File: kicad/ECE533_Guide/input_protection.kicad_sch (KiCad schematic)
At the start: 29 parts, among them J1 DC+ 72V, J3 DC- return, Q1 IPT015N10N5, Q2 IPT015N10N5, U12 LM5069MM-2, U13 VOM1271T, U22 TLV3012

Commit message: Stage 2: BOM from schematic, LCSC numbers, fix duplicate C114 (refs #2)
- kicad/tools/make_bom.py builds bom/PCB_BOM.xlsx (+ CSV) from the netlist;
  previous report BOM kept as a sheet, Digi-Key PNs carried over
- 47 LCSC numbers verified on lcsc.com; two unconfirmed Murata MPNs replaced
- check_netlist.py now also checks for duplicate reference designators
- Yageo part-number codes fixed (13K, 0R jumper)

Co-Authored-By: Claude Opus 5.5 <noreply@anthropic.com>
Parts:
- C70, C71: LCSC (none) -> C5370002; MPN GRM21BR72A105KA01L -> CC0805KKX7R0BB105; Manufacturer Murata -> YAGEO
- C72: LCSC (none) -> C77052
- C73: LCSC (none) -> C77055
- R47: MPN RC0603FR-0713K0L -> RC0603FR-0713KL
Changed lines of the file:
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@@
 		(property "Datasheet" "" (at 111.76 87.63 0) (hide yes) (effects (font (size 1.27 1.27))))
 		(property "Description" "Unpolarized capacitor" (at 111.76 87.63 0) (hide yes) (effects (font (size 1.27 1.27))))
-		(property "MPN" "GRM21BR72A105KA01L" (at 111.76 87.63 0) (hide yes) (effects (font (size 1.27 1.27))))
-		(property "Manufacturer" "Murata" (at 111.76 87.63 0) (hide yes) (effects (font (size 1.27 1.27))))
+		(property "MPN" "CC0805KKX7R0BB105" (at 111.76 87.63 0) (hide yes) (effects (font (size 1.27 1.27))))
+		(property "Manufacturer" "YAGEO" (at 111.76 87.63 0) (hide yes) (effects (font (size 1.27 1.27))))
+		(property "LCSC" "C5370002" (at 111.76 87.63 0) (hide yes) (effects (font (size 1.27 1.27))))
 		(pin "1")
 		(pin "2")
@@
 		(property "Datasheet" "" (at 127 105.41 0) (hide yes) (effects (font (size 1.27 1.27))))
 		(property "Description" "Unpolarized capacitor" (at 127 105.41 0) (hide yes) (effects (font (size 1.27 1.27))))
-		(property "MPN" "GRM21BR72A105KA01L" (at 127 105.41 0) (hide yes) (effects (font (size 1.27 1.27))))
-		(property "Manufacturer" "Murata" (at 127 105.41 0) (hide yes) (effects (font (size 1.27 1.27))))
+		(property "MPN" "CC0805KKX7R0BB105" (at 127 105.41 0) (hide yes) (effects (font (size 1.27 1.27))))
+		(property "Manufacturer" "YAGEO" (at 127 105.41 0) (hide yes) (effects (font (size 1.27 1.27))))
+		(property "LCSC" "C5370002" (at 127 105.41 0) (hide yes) (effects (font (size 1.27 1.27))))
 		(pin "1")
 		(pin "2")
@@
 		(property "MPN" "GRM188R71E474KA12D" (at 198.12 140.97 0) (hide yes) (effects (font (size 1.27 1.27))))
 		(property "Manufacturer" "Murata" (at 198.12 140.97 0) (hide yes) (effects (font (size 1.27 1.27))))
+		(property "LCSC" "C77052" (at 198.12 140.97 0) (hide yes) (effects (font (size 1.27 1.27))))
 		(pin "1")
 		(pin "2")
@@
 		(property "Datasheet" "" (at 208.28 140.97 0) (hide yes) (effects (font (size 1.27 1.27))))
 		(property "Description" "Resistor" (at 208.28 140.97 0) (hide yes) (effects (font (size 1.27 1.27))))
-		(property "MPN" "RC0603FR-0713K0L" (at 208.28 140.97 0) (hide yes) (effects (font (size 1.27 1.27))))
+		(property "MPN" "RC0603FR-0713KL" (at 208.28 140.97 0) (hide yes) (effects (font (size 1.27 1.27))))
 		(property "Manufacturer" "YAGEO" (at 208.28 140.97 0) (hide yes) (effects (font (size 1.27 1.27))))
 		(pin "1")
@@
 		(property "MPN" "GRM188R71H104KA93D" (at 340.36 54.61 0) (hide yes) (effects (font (size 1.27 1.27))))
 		(property "Manufacturer" "Murata" (at 340.36 54.61 0) (hide yes) (effects (font (size 1.27 1.27))))
-		(pin "1")
-		(pin "2")
+		(property "LCSC" "C77055" (at 340.36 54.61 0) (hide yes) (effects (font (size 1.27 1.27))))
+		(pin "1")
+		(pin "2")

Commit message: Stage 3: footprints from datasheets and vendor libraries, 3D-checked (refs #3)
- ECE533_Mods.pretty (drawn from manufacturer datasheets):
  EPC2304 (EPC copper, solder-mask-defined land pattern and stencil),
  TDK ERUC23 (TDK recommended layout), R_2512_Kelvin (Bourns CSS2H-2512
  pads with net-tie sense strips), Littelfuse 456 fuse (+ placeholder STEP)
- ECE533_Vendor library (git-ignored): Wurth REDCUBE 74650194R and the
  SamacSys NME1S0505SC footprint; vendor STEP models referenced from
  kicad/lib/vendor, alignment verified by rendering
- gen_footprints.py regenerates both libraries; check_footprints.py checks
  symbol pins against footprint pads
- Fix D15/D16 BAT54W footprint: SOT-323, not SOD-323 (pin 3 had no pad)
- ERC: 0 violations locally (footprint links now resolve)

Co-Authored-By: Claude Opus 5.5 <noreply@anthropic.com>
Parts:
- J1, J3: footprint ECE533_Mods:Wurth_REDCUBE_74650194 -> ECE533_Vendor:Wurth_REDCUBE_74650194
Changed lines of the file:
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@@
 		(property "Reference" "J1" (at 17.78 80.01 0) (effects (font (size 1.27 1.27)) (justify left)))
 		(property "Value" "DC+ 72V" (at 17.78 82.55 0) (effects (font (size 1.27 1.27)) (justify left)))
-		(property "Footprint" "ECE533_Mods:Wurth_REDCUBE_74650194" (at 35.56 81.28 0) (hide yes) (effects (font (size 1.27 1.27))))
+		(property "Footprint" "ECE533_Vendor:Wurth_REDCUBE_74650194" (at 35.56 81.28 0) (hide yes) (effects (font (size 1.27 1.27))))
 		(property "Datasheet" "" (at 35.56 81.28 0) (hide yes) (effects (font (size 1.27 1.27))))
 		(property "Description" "Generic connector, single row, 01x01, script generated (kicad-library-utils/schlib/autogen/connector/)" (at 35.56 81.28 0) (hide yes) (effects (font (size 1.27 1.27))))
@@
 		(property "Reference" "J3" (at 17.78 110.49 0) (effects (font (size 1.27 1.27)) (justify left)))
 		(property "Value" "DC- return" (at 17.78 113.03 0) (effects (font (size 1.27 1.27)) (justify left)))
-		(property "Footprint" "ECE533_Mods:Wurth_REDCUBE_74650194" (at 35.56 111.76 0) (hide yes) (effects (font (size 1.27 1.27))))
+		(property "Footprint" "ECE533_Vendor:Wurth_REDCUBE_74650194" (at 35.56 111.76 0) (hide yes) (effects (font (size 1.27 1.27))))
 		(property "Datasheet" "" (at 35.56 111.76 0) (hide yes) (effects (font (size 1.27 1.27))))
 		(property "Description" "Generic connector, single row, 01x01, script generated (kicad-library-utils/schlib/autogen/connector/)" (at 35.56 111.76 0) (hide yes) (effects (font (size 1.27 1.27))))

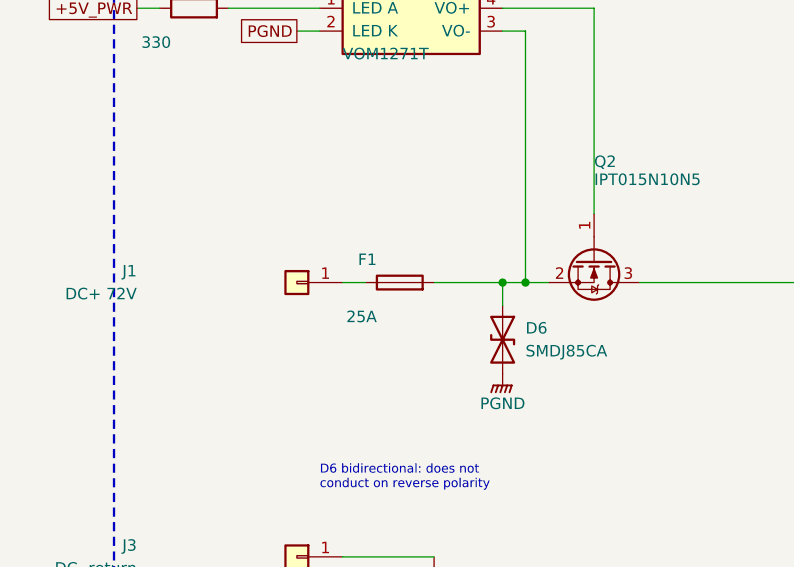
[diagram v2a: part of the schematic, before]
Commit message: Stage 3: input fuse F1 becomes a not-fitted option, R96 link (refs #3)
0456025.ER is rated 72 VDC, below the 79.2 V maximum input, and no
>=25 A SMD fuse rated >=100 VDC was found. Per review decision the
LM5069 circuit breaker is the eFuse; F1 keeps its NANO2 456 footprint
(DNP) and R96 (Bourns CSS2H-2512C-000, <0.1 mOhm, 100 A) links it.
Adds the R_2512_CSS2H footprint; BOM regenerated.

Co-Authored-By: Claude Opus 5.5 <noreply@anthropic.com>
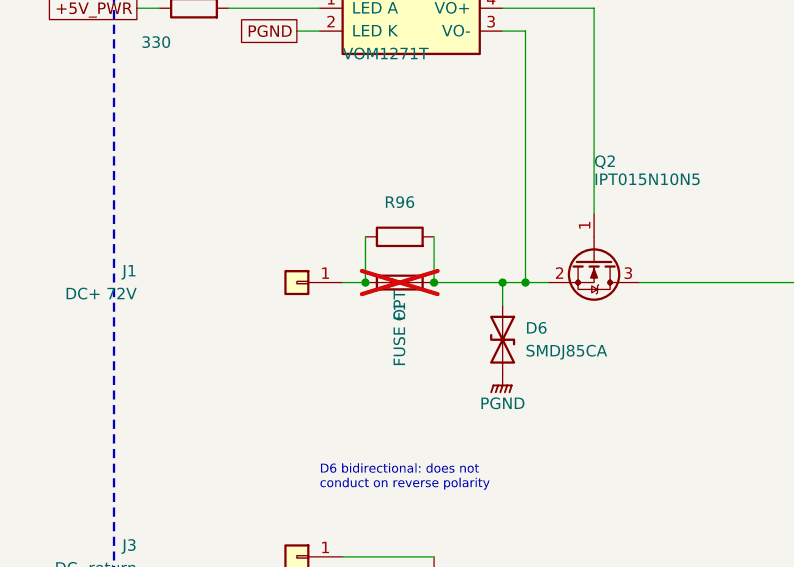
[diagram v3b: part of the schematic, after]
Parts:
- added R96: 0R 100A, ECE533_Mods:R_2512_CSS2H, symbol Device:R
- F1: value 25A -> FUSE OPT; LCSC C315877 -> (none); MPN 0456025.ER -> not fitted; Manufacturer Littelfuse -> (none); now not fitted
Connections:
- net at F1.1, J1.1 (Pin_1): now also R96.1
- net at D6.1 (A1), F1.2, Q2.2 (S)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: now also R96.2
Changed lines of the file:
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@@
 	)
 	(text "INPUT PROTECTION (HV domain):  J1 -> F1 -> D6 -> Q2 (reverse) -> RS1 -> Q1 (hot-swap) -> VBUS" (exclude_from_sim no) (at 20.32 20.32 0) (effects (font (size 1.778 1.778) (bold yes)) (justify left top)))
+	(wire (pts (xy 43.18 81.28) (xy 43.18 76.2)) (stroke (width 0) (type default)))
+	(junction (at 43.18 81.28) (diameter 0) (color 0 0 0 0))
+	(wire (pts (xy 50.8 81.28) (xy 50.8 76.2)) (stroke (width 0) (type default)))
+	(junction (at 50.8 81.28) (diameter 0) (color 0 0 0 0))
 	(wire (pts (xy 40.64 111.76) (xy 50.8 111.76)) (stroke (width 0) (type default)))
 	(wire (pts (xy 40.64 81.28) (xy 43.18 81.28)) (stroke (width 0) (type default)))
@@
 	)
 	(symbol
+		(lib_id "Device:R")
+		(at 46.99 76.2 90)
+		(unit 1)
+		(exclude_from_sim no)
+		(in_bom yes)
+		(on_board yes)
+		(dnp no)
+		(property "Reference" "R96" (at 46.99 72.39 90) (effects (font (size 1.27 1.27))))
+		(property "Value" "0R 100A" (at 46.99 74.295 90) (hide yes) (effects (font (size 1.27 1.27))))
+		(property "Footprint" "ECE533_Mods:R_2512_CSS2H" (at 46.99 76.2 90) (hide yes) (effects (font (size 1.27 1.27))))
+		(property "Datasheet" "https://www.bourns.com/docs/product-datasheets/css2h-2512.pdf" (at 46.99 76.2 90) (hide yes) (effects (font (size 1.27 1.27))))
+		(property "Description" "Input link (< 0.1 mOhm, 100 A); remove when an optional fuse F1 is fitted" (at 46.99 76.2 90) (hide yes) (effects (font (size 1.27 1.27))))
+		(property "MPN" "CSS2H-2512C-000" (at 46.99 76.2 90) (hide yes) (effects (font (size 1.27 1.27))))
+		(property "Manufacturer" "Bourns" (at 46.99 76.2 90) (hide yes) (effects (font (size 1.27 1.27))))
+		(pin "1")
+		(pin "2")
+		(instances (project "ECE533_Guide"
+			(path "/3bc94f09-386f-53fd-bc70-05d96028f503/27028dcf-ec67-5ade-9ed6-3ce4b615d3f0" (reference "R96") (unit 1))
+		))
+	)
+	(symbol
 		(lib_id "Device:Fuse")
 		(at 46.99 81.28 90)
@@
 		(in_bom yes)
 		(on_board yes)
-		(dnp no)
-		(property "Reference" "F1" (at 44.45 78.74 90) (effects (font (size 1.27 1.27)) (justify left)))
-		(property "Value" "25A" (at 44.45 85.09 90) (effects (font (size 1.27 1.27)) (justify left)))
+		(dnp yes)
+		(property "Reference" "F1" (at 46.99 84.455 0) (effects (font (size 1.27 1.27))))
+		(property "Value" "FUSE OPT" (at 46.99 86.36 0) (effects (font (size 1.27 1.27))))
 		(property "Footprint" "ECE533_Mods:Fuse_Littelfuse_NANO2_456" (at 46.99 81.28 90) (hide yes) (effects (font (size 1.27 1.27))))
 		(property "Datasheet" "" (at 46.99 81.28 90) (hide yes) (effects (font (size 1.27 1.27))))
-		(property "Description" "Fuse" (at 46.99 81.28 90) (hide yes) (effects (font (size 1.27 1.27))))
-		(property "MPN" "0456025.ER" (at 46.99 81.28 90) (hide yes) (effects (font (size 1.27 1.27))))
-		(property "Manufacturer" "Littelfuse" (at 46.99 81.28 90) (hide yes) (effects (font (size 1.27 1.27))))
-		(property "LCSC" "C315877" (at 46.99 81.28 90) (hide yes) (effects (font (size 1.27 1.27))))
+		(property "Description" "Optional input fuse, fit only a part rated >= 100 VDC and remove R96" (at 46.99 81.28 90) (hide yes) (effects (font (size 1.27 1.27))))
+		(property "MPN" "not fitted" (at 46.99 81.28 90) (hide yes) (effects (font (size 1.27 1.27))))
+		(property "Manufacturer" "" (at 46.99 81.28 90) (hide yes) (effects (font (size 1.27 1.27))))
 		(pin "1")
 		(pin "2")

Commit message: Stage 3: board set-up, JLCPCB rules and first-pass placement (refs #3)
- build_pcb.py builds the PCB from the netlist: ID-1 outline, 4 x 2 oz
  stack-up (3313, ENIG), layer names, LV_ISO/HV_SW net classes, heatsink,
  pedestal and fan-duct outlines, isolation-barrier rule area, and places
  all 273 footprints (power stage on the bottom under L1, isolators on the
  barrier column, terminals on the right edge)
- ECE533_Guide.kicad_dru: JLC 2 oz limits, HV margin, 2.5 mm barrier rule
- Test points 1.0 mm (all on top); L1 pin-1 mark moved off RS2
- DRC with parity: 0 errors; only unrouted nets and 1 silk warning remain
- docs/design/placement_stage3.md with renders, PROGRESS updated

Co-Authored-By: Claude Opus 5.5 <noreply@anthropic.com>
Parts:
- TP1, TP11: footprint TestPoint:TestPoint_Pad_D1.5mm -> TestPoint:TestPoint_Pad_D1.0mm
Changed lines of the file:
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@@
 		(property "Reference" "TP1" (at 322.58 151.13 0) (effects (font (size 1.27 1.27)) (justify left)))
 		(property "Value" "VBUS" (at 322.58 153.67 0) (effects (font (size 1.27 1.27)) (justify left)))
-		(property "Footprint" "TestPoint:TestPoint_Pad_D1.5mm" (at 320.04 152.4 0) (hide yes) (effects (font (size 1.27 1.27))))
+		(property "Footprint" "TestPoint:TestPoint_Pad_D1.0mm" (at 320.04 152.4 0) (hide yes) (effects (font (size 1.27 1.27))))
 		(property "Datasheet" "" (at 320.04 152.4 0) (hide yes) (effects (font (size 1.27 1.27))))
 		(property "Description" "test point" (at 320.04 152.4 0) (hide yes) (effects (font (size 1.27 1.27))))
@@
 		(property "Reference" "TP11" (at 337.82 151.13 0) (effects (font (size 1.27 1.27)) (justify left)))
 		(property "Value" "PGND" (at 337.82 153.67 0) (effects (font (size 1.27 1.27)) (justify left)))
-		(property "Footprint" "TestPoint:TestPoint_Pad_D1.5mm" (at 335.28 152.4 0) (hide yes) (effects (font (size 1.27 1.27))))
+		(property "Footprint" "TestPoint:TestPoint_Pad_D1.0mm" (at 335.28 152.4 0) (hide yes) (effects (font (size 1.27 1.27))))
 		(property "Datasheet" "" (at 335.28 152.4 0) (hide yes) (effects (font (size 1.27 1.27))))
 		(property "Description" "test point" (at 335.28 152.4 0) (hide yes) (effects (font (size 1.27 1.27))))
